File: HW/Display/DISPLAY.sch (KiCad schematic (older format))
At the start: 17 parts, among them J1 IO, SW1 SW_PUSH, SW2 SW_PUSH, SW3 SW_PUSH, SW4 SW_PUSH, U1 ULN2003A, U2 HDSP-B09G, U3 MCP23017

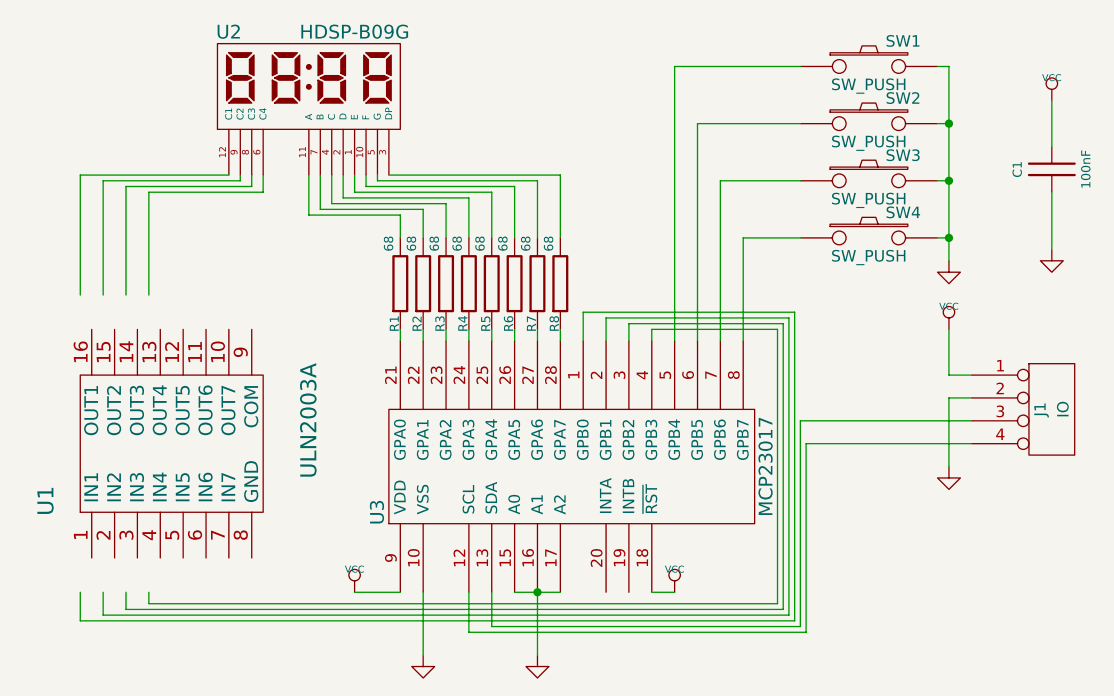
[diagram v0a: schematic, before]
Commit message: Add Display design
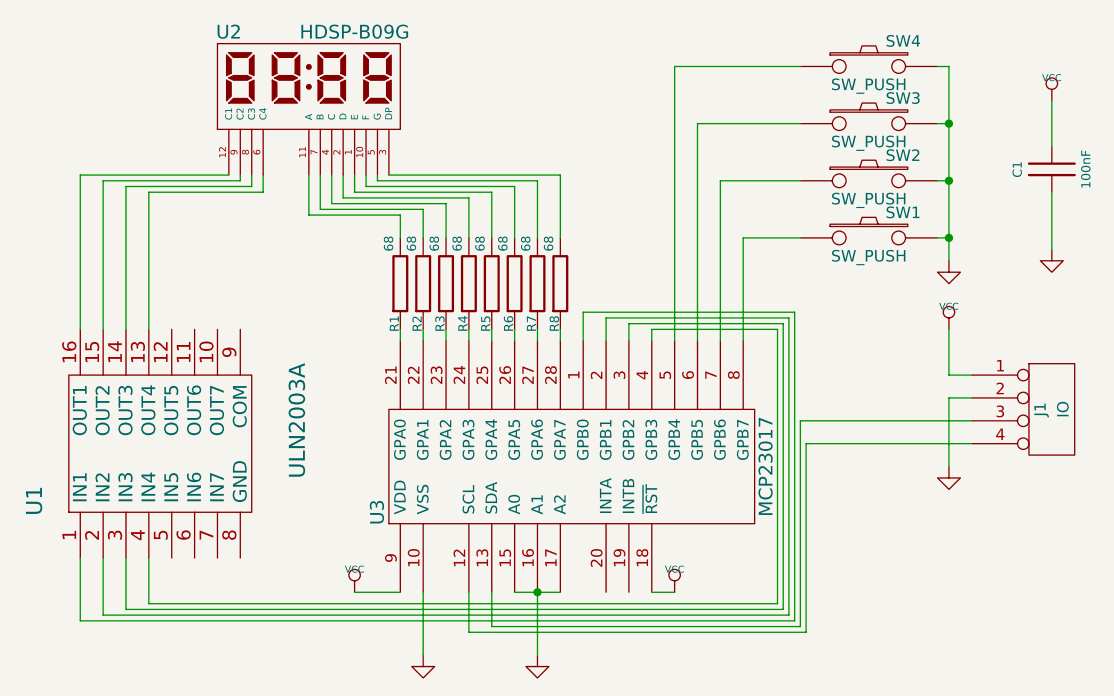
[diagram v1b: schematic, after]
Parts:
- renumbered SW4 to SW1, SW3 to SW2, SW2 to SW3, SW1 to SW4
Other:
- moved on the sheet: U1
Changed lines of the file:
@@
 LIBS:memory
 LIBS:xilinx
-LIBS:special
 LIBS:microcontrollers
 LIBS:dsp
@@
 LIBS:valves
 LIBS:DISPLAY-cache
-EELAYER 27 0
+EELAYER 25 0
 EELAYER END
 $Descr A4 11693 8268
@@
 L ULN2003A U1
 U 1 1 52696E56
-P 4250 3550
-F 0 "U1" H 4000 4100 70  0000 C CNN
-F 1 "ULN2003A" H 4350 2950 70  0000 C CNN
-F 2 "DIP-16__300" H 4250 3550 60  0001 C CNN
-F 3 "" H 4250 3550 60  0000 C CNN
-	1    4250 3550
+P 4200 3550
+F 0 "U1" H 3950 4100 70  0000 C CNN
+F 1 "ULN2003A" H 4300 2950 70  0000 C CNN
+F 2 "DIP-16__300" H 4200 3550 60  0001 C CNN
+F 3 "" H 4200 3550 60  0000 C CNN
+	1    4200 3550
 	0    -1   -1   0
 $EndComp
@@
 	4500 2375 3850 2375
 Wire Wire Line
-	3850 2375 3850 2900
+	3850 2375 3850 3050
 Wire Wire Line
 	4550 2375 4550 2400
@@
 	4550 2400 3950 2400
 Wire Wire Line
-	3950 2400 3950 2900
+	3950 2400 3950 3050
 Wire Wire Line
 	4600 2375 4600 2425
@@
 	4600 2425 4050 2425
 Wire Wire Line
-	4050 2425 4050 2900
-Wire Wire Line
-	4150 2450 4150 2900
+	4050 2425 4050 3050
+Wire Wire Line
+	4150 2450 4150 3050
 Wire Wire Line
 	4150 2450 4650 2450
@@
 	6900 4250 4150 4250
 Wire Wire Line
-	4150 4250 4150 4200
-Wire Wire Line
-	4050 4200 4050 4275
+	4150 4250 4150 4050
+Wire Wire Line
+	4050 4050 4050 4275
 Wire Wire Line
 	4050 4275 6925 4275
@@
 	6950 4300 3950 4300
 Wire Wire Line
-	3950 4300 3950 4200
-Wire Wire Line
-	3850 4200 3850 4325
+	3950 4300 3950 4050
+Wire Wire Line
+	3850 4050 3850 4325
 Wire Wire Line
 	3850 4325 6975 4325
@@
 	5550 4375 5550 4200
 $Comp
-L SW_PUSH SW1
+L SW_PUSH SW4
 U 1 1 52761E18
 P 7300 1900
-F 0 "SW1" H 7450 2010 50  0000 C CNN
+F 0 "SW4" H 7450 2010 50  0000 C CNN
 F 1 "SW_PUSH" H 7300 1820 50  0000 C CNN
 F 2 "SW_PUSH_SMALL" H 7300 1900 60  0001 C CNN
@@
 $EndComp
 $Comp
-L SW_PUSH SW2
+L SW_PUSH SW3
 U 1 1 52761E7A
 P 7300 2150
-F 0 "SW2" H 7450 2260 50  0000 C CNN
+F 0 "SW3" H 7450 2260 50  0000 C CNN
 F 1 "SW_PUSH" H 7300 2070 50  0000 C CNN
 F 2 "SW_PUSH_SMALL" H 7300 2150 60  0001 C CNN
@@
 $EndComp
 $Comp
-L SW_PUSH SW3
+L SW_PUSH SW2
 U 1 1 52761E89
 P 7300 2400
-F 0 "SW3" H 7450 2510 50  0000 C CNN
+F 0 "SW2" H 7450 2510 50  0000 C CNN
 F 1 "SW_PUSH" H 7300 2320 50  0000 C CNN
 F 2 "SW_PUSH_SMALL" H 7300 2400 60  0001 C CNN
@@
 $EndComp
 $Comp
-L SW_PUSH SW4
+L SW_PUSH SW1
 U 1 1 52761E98
 P 7300 2650
-F 0 "SW4" H 7450 2760 50  0000 C CNN
+F 0 "SW1" H 7450 2760 50  0000 C CNN
 F 1 "SW_PUSH" H 7300 2570 50  0000 C CNN
 F 2 "SW_PUSH_SMALL" H 7300 2650 60  0001 C CNN
@@
 Connection ~ 7650 2650
 $Comp
-L GND #PWR?
+L GND #PWR08
 U 1 1 52797EE5
 P 8100 2700
-F 0 "#PWR?" H 8100 2700 30  0001 C CNN
+F 0 "#PWR08" H 8100 2700 30  0001 C CNN
 F 1 "GND" H 8100 2630 30  0001 C CNN
 F 2 "" H 8100 2700 60  0000 C CNN
@@
 $EndComp
 $Comp
-L VCC #PWR?
+L VCC #PWR09
 U 1 1 52797EF4
 P 8100 2050
-F 0 "#PWR?" H 8100 2150 30  0001 C CNN
+F 0 "#PWR09" H 8100 2150 30  0001 C CNN
 F 1 "VCC" H 8100 2150 30  0000 C CNN
 F 2 "" H 8100 2050 60  0000 C CNN
